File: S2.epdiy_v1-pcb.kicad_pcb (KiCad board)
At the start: 4 copper layers, 106.6 x 58.9 mm, 82 parts, among them J1 USB_C_Receptacle_USB2.0, J2 Jack-DC, P1 CONN_02X13, SW1 RESET, SW2 BOOT, U1 MCP1700-1202E_SOT23, U11 TP4056, U2 ESP32-S2-WROVER, U3 TPS651851RSLR, U6 ED060XC5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

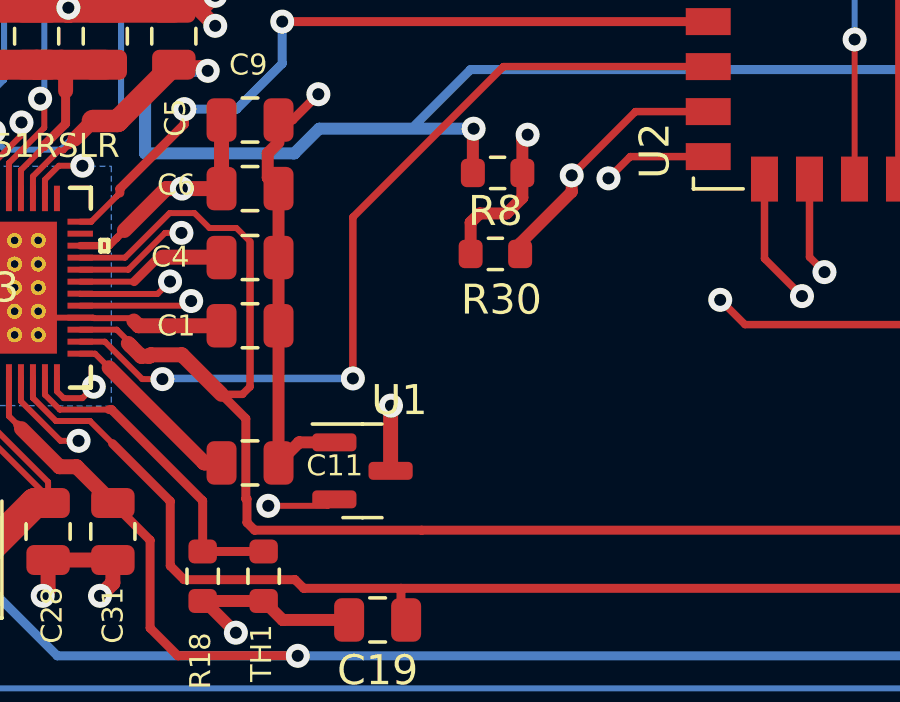
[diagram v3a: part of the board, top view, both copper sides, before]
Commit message: Add 470uF C at LDO 3.3v output
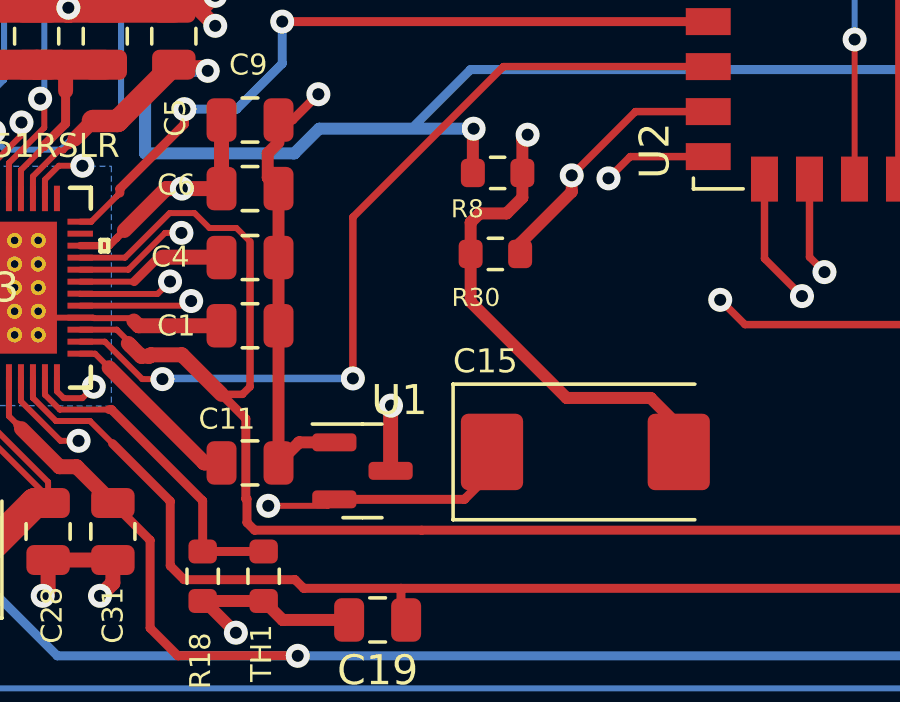
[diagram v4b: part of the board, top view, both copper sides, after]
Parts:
- added C15: C_Polarized, Capacitor_Tantalum_SMD:CP_EIA-7343-43_Kemet-X, F.Cu at (150.4, 111.5)
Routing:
- net GND: track 290.6 -> 301.7 mm
- net /+3.3V: track 78.2 -> 84.5 mm
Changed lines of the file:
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@@
     )
   )
+  (footprint "Capacitor_Tantalum_SMD:CP_EIA-7343-43_Kemet-X" (layer "F.Cu")
+    (at 150.45 111.45)
+    (descr "Tantalum Capacitor SMD Kemet-X (7343-43 Metric), IPC_7351 nominal, (Body size from: http://www.kemet.com/Lists/ProductCatalog/Attachments/253/KEM_TC101_STD.pdf), generated with kicad-footprint-generator")
+    (tags "capacitor tantalum")
+    (property "LCSC" "C513339")
+    (property "Sheetfile" "S2.epdiy_v1-pcb.kicad_sch")
+    (property "Sheetname" "")
+    (attr smd)
+    (fp_text reference "C15" (at -3.334523 -3.025) (layer "F.SilkS")
+      (effects (font (size 0.8 0.8) (thickness 0.15)))
+    )
+    (fp_text value "C_Polarized" (at 0 3.1) (layer "F.Fab")
+      (effects (font (size 1 1) (thickness 0.15)))
+    )
+    (fp_text user "${REFERENCE}" (at 0 0) (layer "F.Fab")
+      (effects (font (size 1 1) (thickness 0.15)))
+    )
+    (fp_line (start -4.41 -2.26) (end -4.41 2.26) (layer "F.SilkS") (width 0.12))
+    (fp_line (start 3.65 -2.26) (end -4.41 -2.26) (layer "F.SilkS") (width 0.12))
+    (fp_line (start -4.41 2.26) (end 3.65 2.26) (layer "F.SilkS") (width 0.12))
+    (fp_line (start 4.4 2.4) (end -4.4 2.4) (layer "F.CrtYd") (width 0.05))
+    (fp_line (start -4.4 -2.4) (end 4.4 -2.4) (layer "F.CrtYd") (width 0.05))
+    (fp_line (start -4.4 2.4) (end -4.4 -2.4) (layer "F.CrtYd") (width 0.05))
+    (fp_line (start 4.4 -2.4) (end 4.4 2.4) (layer "F.CrtYd") (width 0.05))
+    (fp_line (start 3.65 2.15) (end 3.65 -2.15) (layer "F.Fab") (width 0.1))
+    (fp_line (start 3.65 -2.15) (end -2.65 -2.15) (layer "F.Fab") (width 0.1))
+    (fp_line (start -2.65 -2.15) (end -3.65 -1.15) (layer "F.Fab") (width 0.1))
+    (fp_line (start -3.65 2.15) (end 3.65 2.15) (layer "F.Fab") (width 0.1))
+    (fp_line (start -3.65 -1.15) (end -3.65 2.15) (layer "F.Fab") (width 0.1))
+    (pad "1" smd roundrect (at -3.1125 0) (size 2.075 2.55) (layers "F.Cu" "F.Paste" "F.Mask") (roundrect_rratio 0.120482)
+      (net 96 "/+3.3V") (pintype "passive"))
+    (pad "2" smd roundrect (at 3.1125 0) (size 2.075 2.55) (layers "F.Cu" "F.Paste" "F.Mask") (roundrect_rratio 0.120482)
+      (net 1 "GND") (pintype "passive"))
+    (model "${KICAD6_3DMODEL_DIR}/Capacitor_Tantalum_SMD.3dshapes/CP_EIA-7343-43_Kemet-X.wrl"
+      (offset (xyz 0 0 0))
+      (scale (xyz 1 1 1))
+      (rotate (xyz 0 0 0))
+    )
+  )
   (footprint "Capacitor_SMD:C_1206_3216Metric" (layer "F.Cu")
     (at 111.225 106.625 180)
@@
     (property "Sheetname" "")
     (attr smd)
-    (fp_text reference "R30" (at 0.125 4.225) (layer "F.SilkS")
-      (effects (font (size 1 1) (thickness 0.15)))
+    (fp_text reference "R30" (at -0.725 4.155) (layer "F.SilkS")
+      (effects (font (size 0.6 0.6) (thickness 0.1)))
     )
     (fp_text value "100k" (at 0 1.43) (layer "F.Fab")
@@
     (property "Sheetname" "")
     (attr smd)
-    (fp_text reference "C11" (at -2.8194 -0.0889) (layer "F.SilkS")
+    (fp_text reference "C11" (at 0.772 1.466) (layer "F.SilkS")
       (effects (font (size 0.7 0.7) (thickness 0.12)))
     )
@@
     (property "Sheetname" "")
     (attr smd)
-    (fp_text reference "R8" (at 0 -1.43) (layer "F.SilkS")
-      (effects (font (size 1 1) (thickness 0.15)))
+    (fp_text reference "R8" (at -0.935714 -1.5) (layer "F.SilkS")
+      (effects (font (size 0.6 0.6) (thickness 0.1)))
     )
     (fp_text value "10K" (at 0 1.43) (layer "F.Fab")
@@
   (segment (start 132.541 116.067) (end 132.362 116.246) (width 0.5) (layer "F.Cu") (net 1))
   (segment (start 121.05 85.35) (end 123.375 85.35) (width 0.4) (layer "F.Cu") (net 1))
+  (segment (start 152.625 109.65) (end 153.5625 110.5875) (width 0.4) (layer "F.Cu") (net 1))
   (segment (start 140.222 104.9707) (end 140.222 107.244) (width 0.4) (layer "F.Cu") (net 1))
   (segment (start 148.35 102.15) (end 148.35 101.05) (width 0.4) (layer "F.Cu") (net 1))
@@
   (segment (start 178.575 112.9) (end 178.925 112.9) (width 0.25) (layer "F.Cu") (net 1))
   (segment (start 191.145 107.205) (end 191.195 107.255) (width 0.25) (layer "F.Cu") (net 1))
+  (segment (start 149.825 109.65) (end 152.625 109.65) (width 0.4) (layer "F.Cu") (net 1))
   (segment (start 169.92 102.355) (end 169.92 103.245) (width 0.3) (layer "F.Cu") (net 1))
   (segment (start 133.216 96.642) (end 136.732 96.642) (width 1) (layer "F.Cu") (net 1))
@@
   (segment (start 136.732 96.642) (end 137.508 96.642) (width 0.5) (layer "F.Cu") (net 1))
   (segment (start 190.645 106.205) (end 191.195 105.655) (width 0.25) (layer "F.Cu") (net 1))
+  (segment (start 153.5625 110.5875) (end 153.5625 111.45) (width 0.4) (layer "F.Cu") (net 1))
   (segment (start 134.7 115.052) (end 134.7 115.816999) (width 0.5) (layer "F.Cu") (net 1))
   (segment (start 117.362 94.246) (end 117.862 93.746) (width 0.5) (layer "F.Cu") (net 1))
@@
   (segment (start 94.4675 98.475) (end 93.495 97.5025) (width 0.4) (layer "F.Cu") (net 1))
   (segment (start 137.9 92.875) (end 137.9 91.45) (width 0.4) (layer "F.Cu") (net 1))
+  (segment (start 146.625 106.45) (end 149.825 109.65) (width 0.4) (layer "F.Cu") (net 1))
   (segment (start 126.812 93.146) (end 127.22201 93.55601) (width 0.5) (layer "F.Cu") (net 1))
   (segment (start 128.35 96.642) (end 129.466 96.642) (width 1) (layer "F.Cu") (net 1))
+  (segment (start 146.625 104.85) (end 146.625 106.45) (width 0.4) (layer "F.Cu") (net 1))
   (segment (start 191.195 105.655) (end 191.195 97.48) (width 0.25) (layer "F.Cu") (net 1))
   (segment (start 97.675 89.75) (end 100.65 89.75) (width 0.4) (layer "F.Cu") (net 1))
@@
   (segment (start 132.954737 111.079) (end 133.557 111.079) (width 0.2) (layer "F.Cu") (net 96))
   (segment (start 141.625 92.3) (end 142.425 93.1) (width 0.3) (layer "F.Cu") (net 96))
+  (segment (start 147.3375 111.45) (end 147.3375 112.1125) (width 0.3) (layer "F.Cu") (net 96))
   (segment (start 133.85 79.24) (end 135.29 79.24) (width 0.3) (layer "F.Cu") (net 96))
   (segment (start 141.625 89.8) (end 141.625 92.3) (width 0.3) (layer "F.Cu") (net 96))
@@
   (segment (start 131.636001 108.949) (end 131.636001 109.760264) (width 0.2) (layer "F.Cu") (net 96))
   (segment (start 139.879874 113.246) (end 141.8665 113.246) (width 0.2) (layer "F.Cu") (net 96))
+  (segment (start 147.3375 112.1125) (end 146.42 113.03) (width 0.3) (layer "F.Cu") (net 96))
   (segment (start 154.545 80.605) (end 146.195 80.605) (width 0.4) (layer "F.Cu") (net 96))
   (segment (start 131.636001 109.760264) (end 132.954737 111.079) (width 0.2) (layer "F.Cu") (net 96))
+  (segment (start 146.42 113.03) (end 142.0825 113.03) (width 0.3) (layer "F.Cu") (net 96))
   (via (at 146.12 80.68) (size 0.8) (drill 0.4) (layers "F.Cu" "B.Cu") (net 96))
   (via (at 139.879874 113.246) (size 0.8) (drill 0.4) (layers "F.Cu" "B.Cu") (net 96))

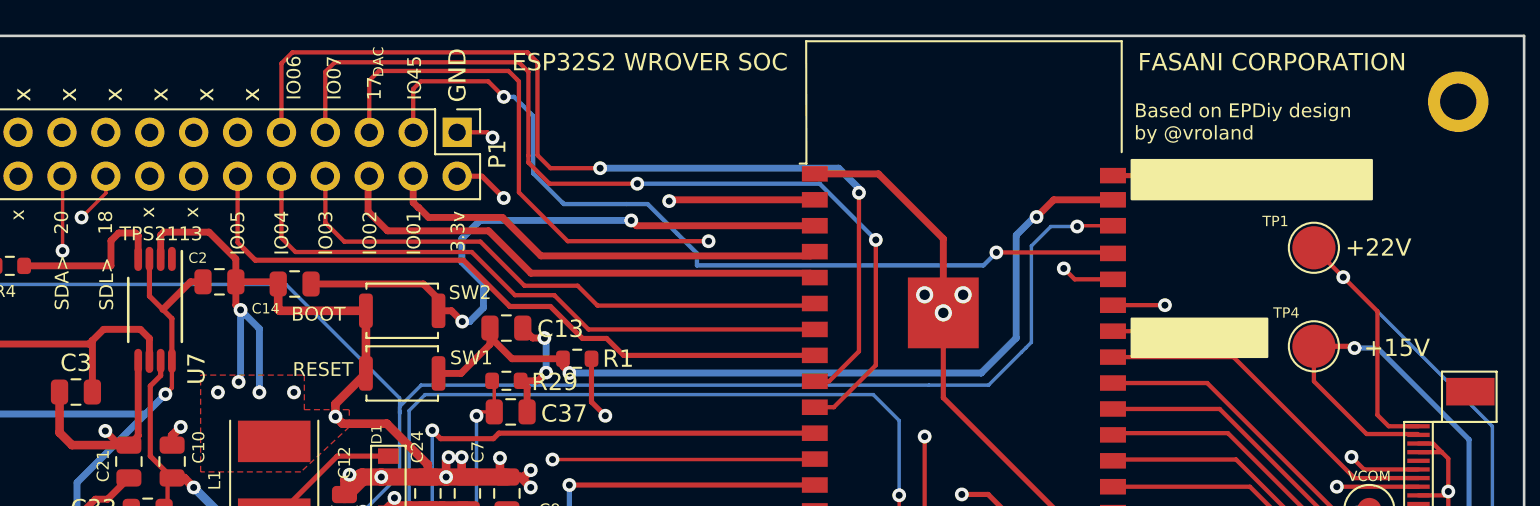
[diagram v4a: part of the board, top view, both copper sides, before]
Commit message: Cooper out of Antenna
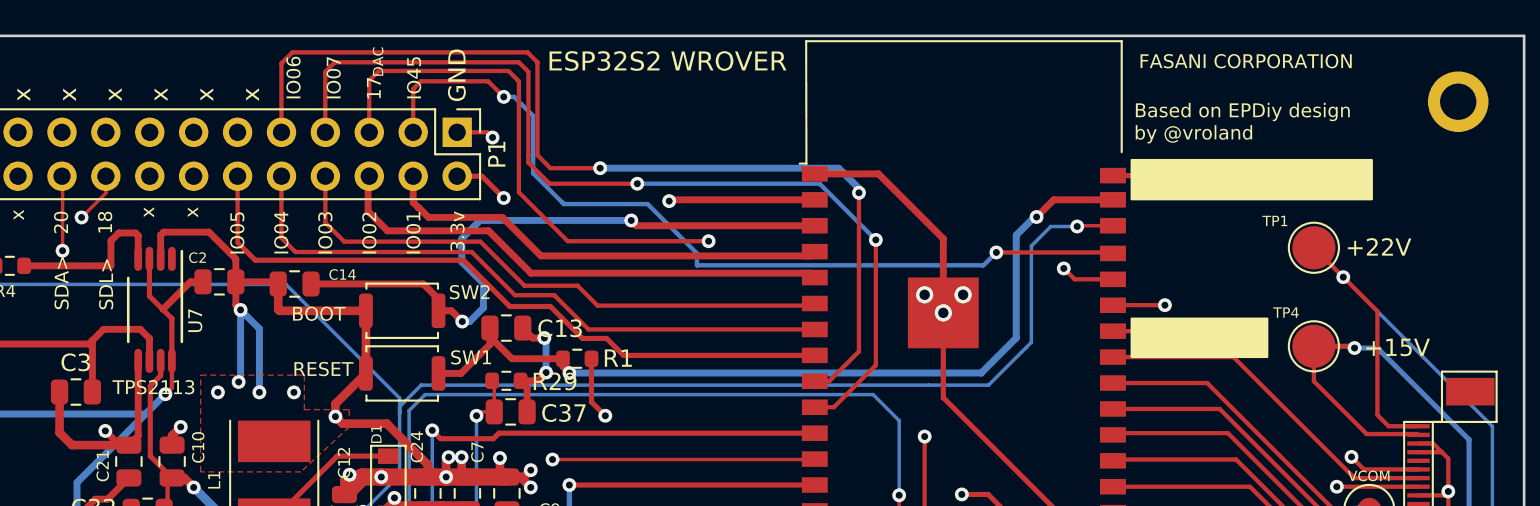
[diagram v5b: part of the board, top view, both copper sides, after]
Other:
- board text added: "ESP32S2 WROVER"
- board text removed: "ESP32S2 WROVER SOC"
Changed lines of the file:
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@@
     (property "Sheetname" "")
     (attr through_hole)
-    (fp_text reference "U7" (at 3.4 -2.4 90) (layer "F.SilkS")
-      (effects (font (size 1 1) (thickness 0.15)))
+    (fp_text reference "U7" (at 0.625 -2.35 90) (layer "F.SilkS")
+      (effects (font (size 0.8 0.8) (thickness 0.1)))
     )
     (fp_text value "TPS2113APW" (at -1.1 -4.5 90) (layer "F.SilkS") hide
@@
     (property "Sheetname" "")
     (attr smd)
-    (fp_text reference "C14" (at -1.675 1.425) (layer "F.SilkS")
+    (fp_text reference "C14" (at 2.775 -0.525) (layer "F.SilkS")
       (effects (font (size 0.6 0.6) (thickness 0.15)))
     )
@@
     (effects (font (size 1 1) (thickness 0.15)))
   )
-  (gr_text "FASANI CORPORATION" (at 181 72.65) (layer "F.SilkS")
-    (effects (font (size 1 1) (thickness 0.15)))
+  (gr_text "FASANI CORPORATION" (at 179.5 72.6145) (layer "F.SilkS")
+    (effects (font (size 0.8 0.8) (thickness 0.1)))
   )
   (gr_text "17" (at 129.06416 74.159523 90) (layer "F.SilkS")
     (effects (font (size 0.8 0.8) (thickness 0.15)))
   )
-  (gr_text "TPS2113" (at 116.725 82.575) (layer "F.SilkS")
+  (gr_text "TPS2113" (at 116.325 91.475) (layer "F.SilkS")
     (effects (font (size 0.8 0.8) (thickness 0.15)))
   )
@@
     (effects (font (size 1 1) (thickness 0.15)))
   )
-  (gr_text "ESP32S2 WROVER SOC" (at 145 72.65) (layer "F.SilkS")
-    (effects (font (size 1 1) (thickness 0.15)))
+  (gr_text "ESP32S2 WROVER" (at 146 72.6145) (layer "F.SilkS")
+    (effects (font (size 1.1 1.1) (thickness 0.12)))
   )
   (gr_text "+22V" (at 187.15 83.375) (layer "F.SilkS")
@@
     (effects (font (size 0.8 0.8) (thickness 0.15)))
   )
-  (gr_text "Based on EPDiy design\nby @vroland" (at 173.025 76.1) (layer "F.SilkS")
-    (effects (font (size 0.8 0.8) (thickness 0.15)) (justify left))
+  (gr_text "Based on EPDiy design\nby @vroland" (at 173.011905 76.1) (layer "F.SilkS")
+    (effects (font (size 0.8 0.8) (thickness 0.1)) (justify left))
   )
   (gr_text "SDA>" (at 111 85.4 90) (layer "F.SilkS")
@@
       (pts
         (xy 196.57 130.53)
-        (xy 89.425 130.425)
-        (xy 89.675 70.725)
-        (xy 196.195 70.355)
+        (xy 88.825 130.225)
+        (xy 88.675 70.6)
+        (xy 139.5 70.6)
+        (xy 139.475 77.675)
+        (xy 187.45 77.825)
+        (xy 187.425 70.45)
+        (xy 196.175 70.45)
       )
     )
@@
       (pts
         (xy 197.125 130.9)
-        (xy 88.9 130.85)
-        (xy 89.175 70.375)
-        (xy 196.8 69.875)
+        (xy 88.4 130.675)
+        (xy 88.425 70.25)
+        (xy 138.925 70.1)
+        (xy 138.925 78.325)
+        (xy 187.575 78.175)
+        (xy 187.575 69.975)
+        (xy 196.775 69.95)
       )
     )

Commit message: Update schematic
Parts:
- U3: value TPS651851RSLR -> TPS65185
- U7: value TPS2113APW -> Val**

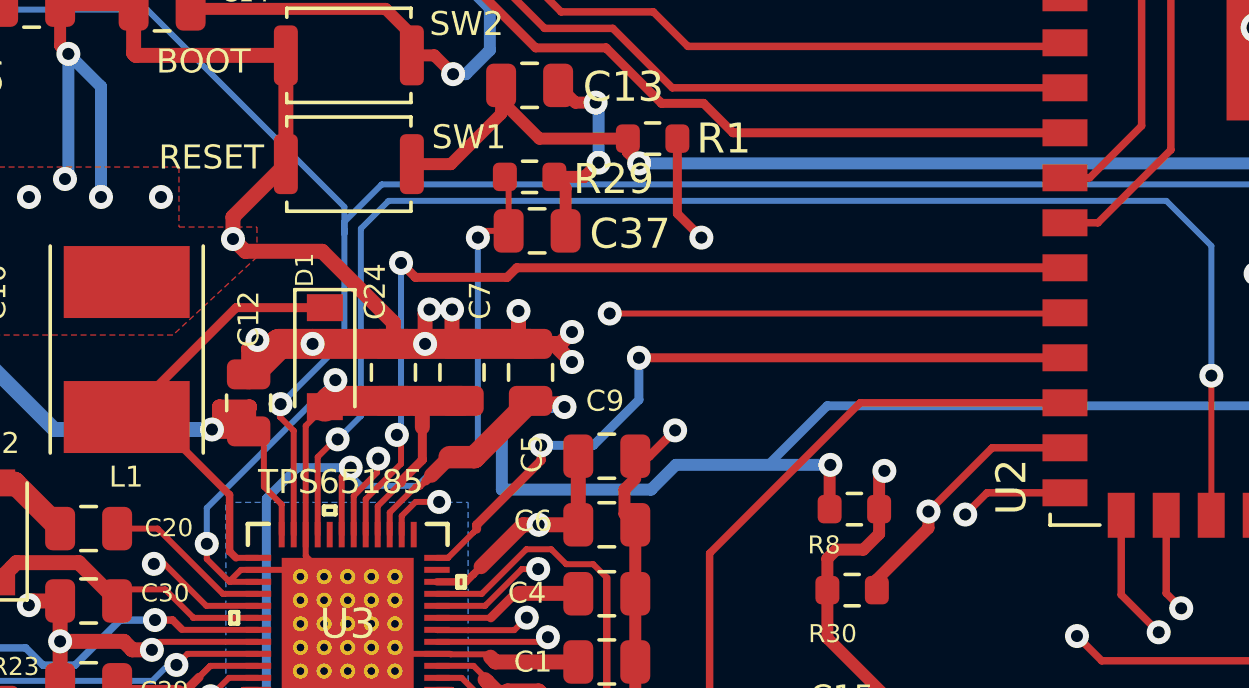
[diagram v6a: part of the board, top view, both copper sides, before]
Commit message: I2C pullups
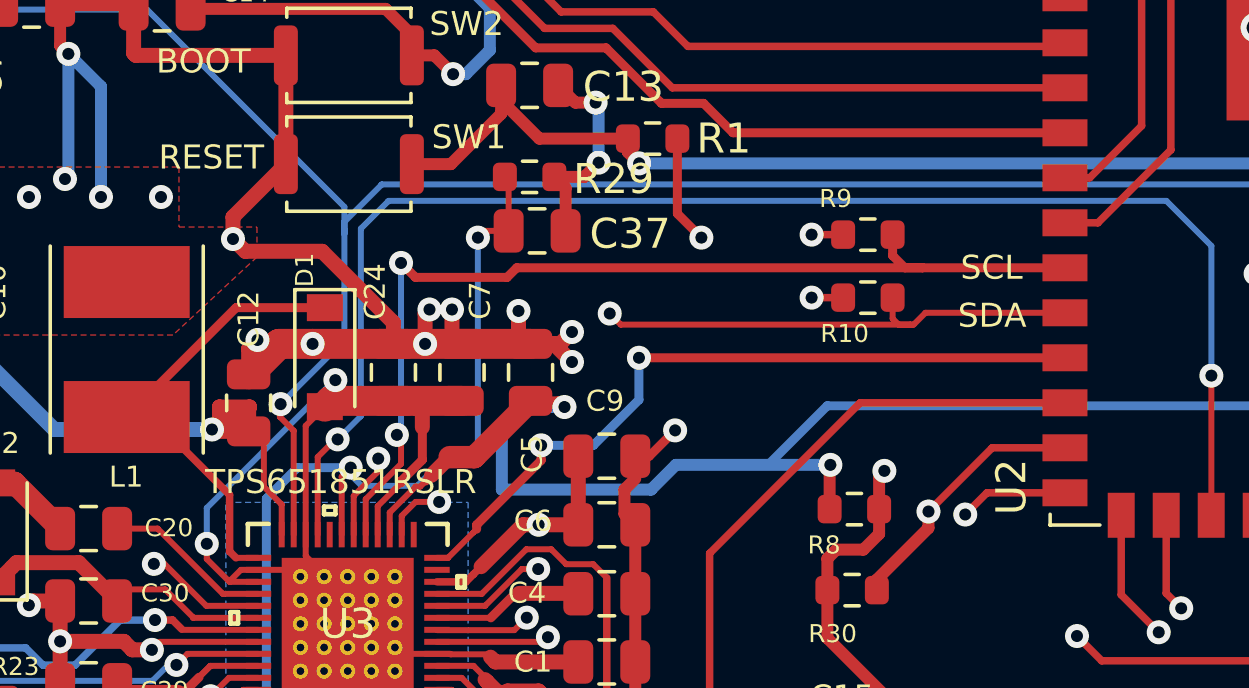
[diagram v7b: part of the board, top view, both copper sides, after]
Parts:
- added R10: 2K2, Resistor_SMD:R_0603_1608Metric, F.Cu at (148.0, 95.1)
- added R9: 2K2, Resistor_SMD:R_0603_1608Metric, F.Cu at (148.0, 93.0)
- U2: footprint footprint:ESP32-S2-WROVER -> RF_Module:ESP32-S2-WROVER
- U3: value TPS65185 -> TPS651851RSLR
- U7: value Val** -> TPS2113APW
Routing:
- net /+3.3V: track 84.5 -> 89.5 mm, vias 5 -> 7
- net /SCL: track 60.8 -> 62.7 mm
- net /SDA: track 64.7 -> 66.4 mm
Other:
- board text added: "SCL"
- board text added: "SDA"

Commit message: DRC passes
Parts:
- removed C21: 0.1uF, Capacitor_SMD:C_0805_2012Metric
- removed MK1, MK2 (x2), MK3: Mounting_Hole, Mounting_Holes:MountingHole_3-5mm
- added H1: MountingHole, MountingHole:MountingHole_2.5mm, F.Cu at (92.9, 75.5)
- added H2: MountingHole, MountingHole:MountingHole_2.5mm, F.Cu at (191.3, 75.5)
- added H3: MountingHole, MountingHole:MountingHole_2.5mm, F.Cu at (92.9, 125.5)
- added H4: MountingHole, MountingHole:MountingHole_2.5mm, F.Cu at (191.3, 125.5)
- U3: value TPS651851RSLR -> QFN50P700X700X100-49N; footprint footprint:TPS651851RSLR -> footprint:TPS65185RGZR_700X700X100-49N
- moved D5 0.93 mm to (118.9, 113.0)
- moved C4 0.83 mm to (140.1, 105.0)
- moved U3 0.70 mm to (130.4, 105.3)
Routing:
- net /VNEG_IN: track 38.3 -> 27.8 mm
- net VBUS: track 94.4 -> 89.4 mm, vias 7 -> 6
- net /-15V: track 91.2 -> 86.2 mm
- net Net-(C26-Pad2): track 34.2 -> 29.5 mm
- net GND: track 301.7 -> 305.9 mm, vias 44 -> 40
- net Net-(D1-Pad1): track 17.8 -> 13.7 mm
- net /15V: track 157.4 -> 154.5 mm
- net /EP_VCOM: track 82.6 -> 80.0 mm, vias 4 -> 5
- net Net-(R19-Pad2): track 23.9 -> 22.1 mm
- net Net-(C29-Pad2): track 12.5 -> 10.9 mm
- net /TPS_PWR_GOOD: track 96.8 -> 95.6 mm
- net /SCL: track 62.7 -> 61.5 mm
- net Net-(C20-Pad2): track 5.61 -> 4.57 mm
- net /-20V: track 109.5 -> 108.5 mm
- net Net-(C25-Pad1): track 6.71 -> 7.66 mm
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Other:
- board text added: "EPDiy S2 v 1.0"
- board text removed: "ESP32S2 WROVER"
